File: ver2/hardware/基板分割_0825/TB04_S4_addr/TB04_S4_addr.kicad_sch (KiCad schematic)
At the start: 12 parts, among them J101 USB_C_Receptacle_PowerOnly_6P, SW101 SW_SPDT, U101 74LS157, U102 74HC138

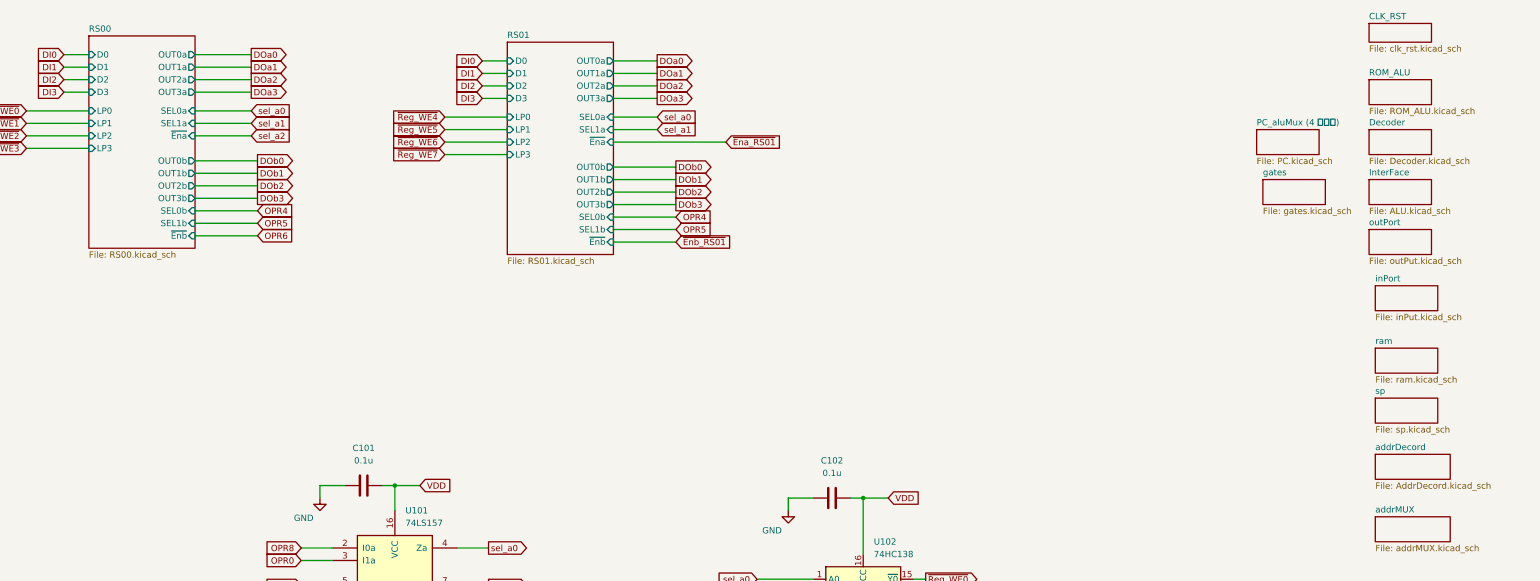
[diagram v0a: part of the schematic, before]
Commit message: ver2: 残り5プロジェクトの不要シートを一括削除
IF表示13/S4 10/S3 11/S1 12/S2 10枚のsheetブロックをS式単位で除去し、
対応する子シート56ファイルを削除。部分削除が要るROM_ALU・PCは残した。
残ったブロックは全てHEADとバイト一致・括弧バランス0を全数確認。

Co-Authored-By: Claude Opus 5 <noreply@anthropic.com>
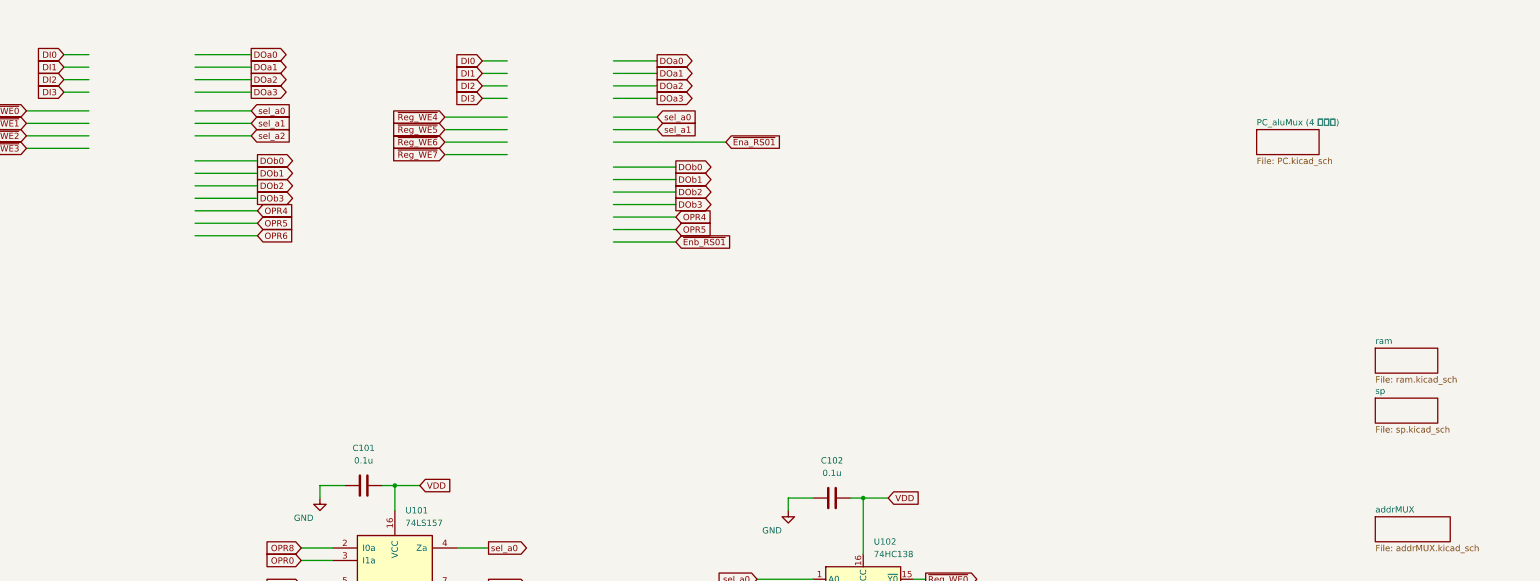
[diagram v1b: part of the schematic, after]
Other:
- removed sheet CLK_RST
- removed sheet Decoder
- removed sheet InterFace
- removed sheet ROM_ALU
- removed sheet RS00
- removed sheet RS01
- removed sheet addrDecord
- removed sheet gates
- removed sheet inPort
- removed sheet outPort

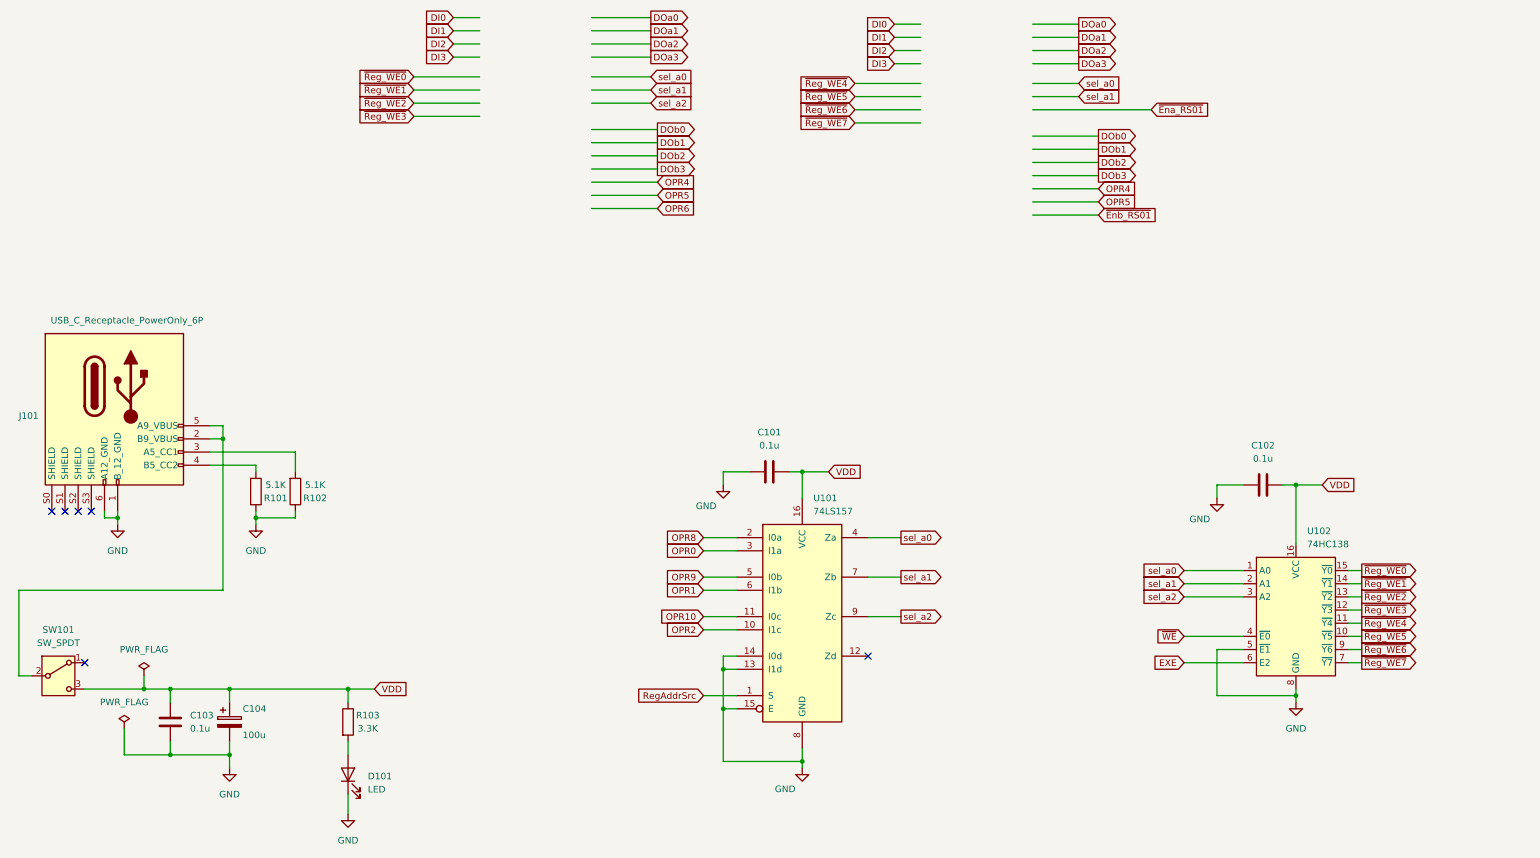
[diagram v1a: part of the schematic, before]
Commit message: ver2: S1-S4のシート内部分削除が完了(署名相違ゼロ)
ROM_ALUをS1(命令ROM側)とS2(ALU ROM・フラグ側)に、PCをS3(ALU入力MUX)と
S4(PC系)に分割。4基板1320ピンをマスターと署名比較して相違0・
ANOMALIES 0。パスコンの員数もIC数と一致(S1 7/S2 17/S3 22/S4 15)。

Co-Authored-By: Claude Opus 5 <noreply@anthropic.com>
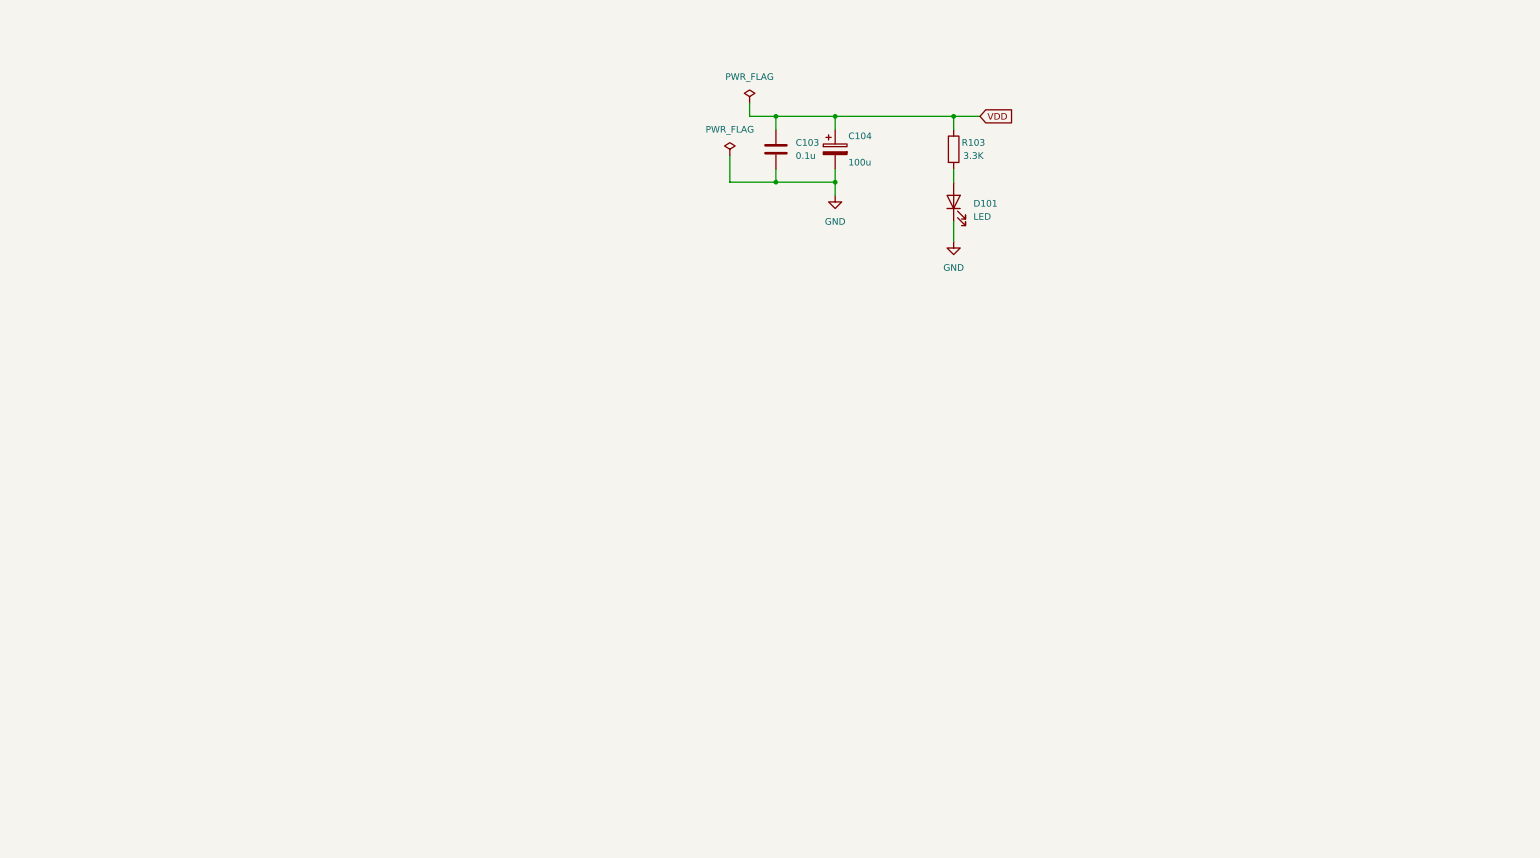
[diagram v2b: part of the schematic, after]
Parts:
- removed C101, C102: 0.1u, Capacitor_THT:C_Disc_D4.3mm_W1.9mm_P5.00mm, symbol Device:C
- removed J101: USB_C_Receptacle_PowerOnly_6P, Library:USB_C_receptacle_onlypower_tanuki, symbol New_Library:USB_C_Receptacle_PowerOnly_6P_tanuki
- removed R101, R102: 5.1K, Resistor_THT:R_Axial_DIN0207_L6.3mm_D2.5mm_P10.16mm_Horizontal, symbol Device:R
- removed SW101: SW_SPDT, Library:sw_slide, symbol Switch:SW_SPDT
- removed U101: 74LS157, symbol 74xx:74LS157
- removed U102: 74HC138, Package_DIP:DIP-16_W7.62mm_Socket, symbol 74xx:74HC138
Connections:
- no-connect marks 6 -> 0
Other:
- moved on the sheet: C103, C104, D101, R103

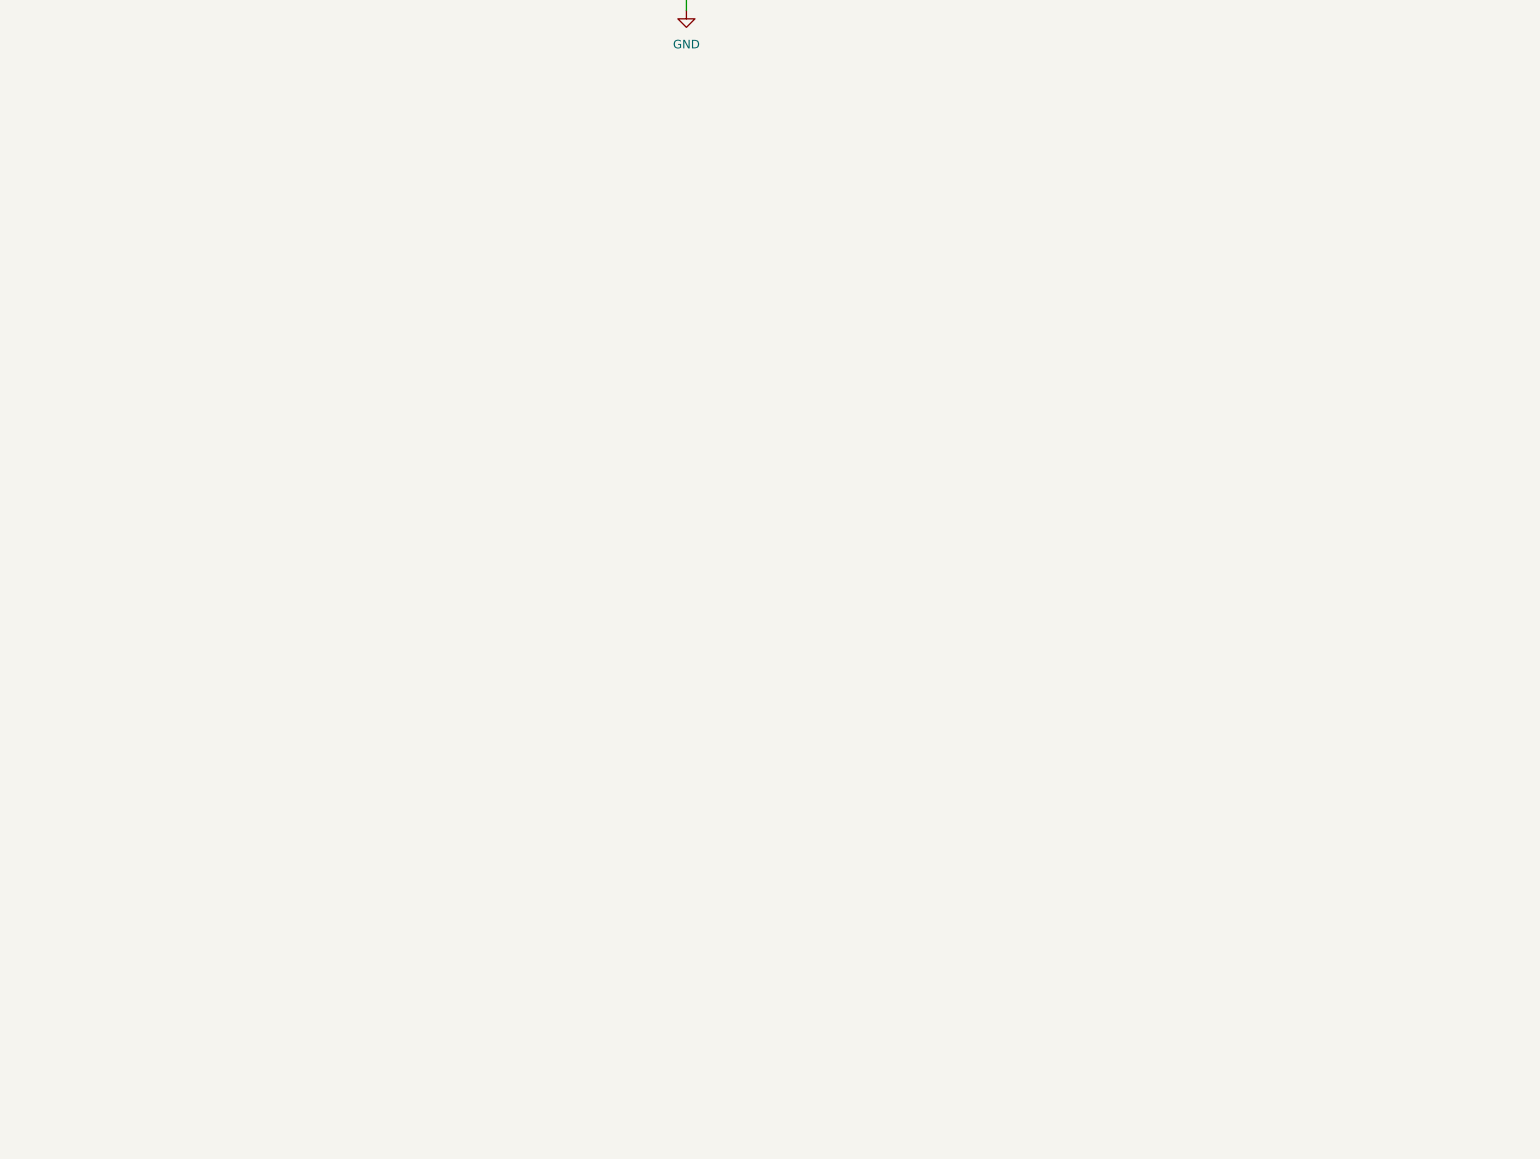
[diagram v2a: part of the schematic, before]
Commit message: ver2: S1-S4にバスヘッダ3本を実装(120ピン全数一致)／S4にIF向け20ピン3個
J101-103は4枚とも確定表と全120ピン一致。J104(IF入力)/J105(IF表示)/
J106(キャリアB)も20ピン全一致。コネクタ以外の署名はマスターと相違0で、
コネクタ追加時のワイヤ吸着なし。PC_Qはバスに載せずJ106のみ。

Co-Authored-By: Claude Opus 5 <noreply@anthropic.com>
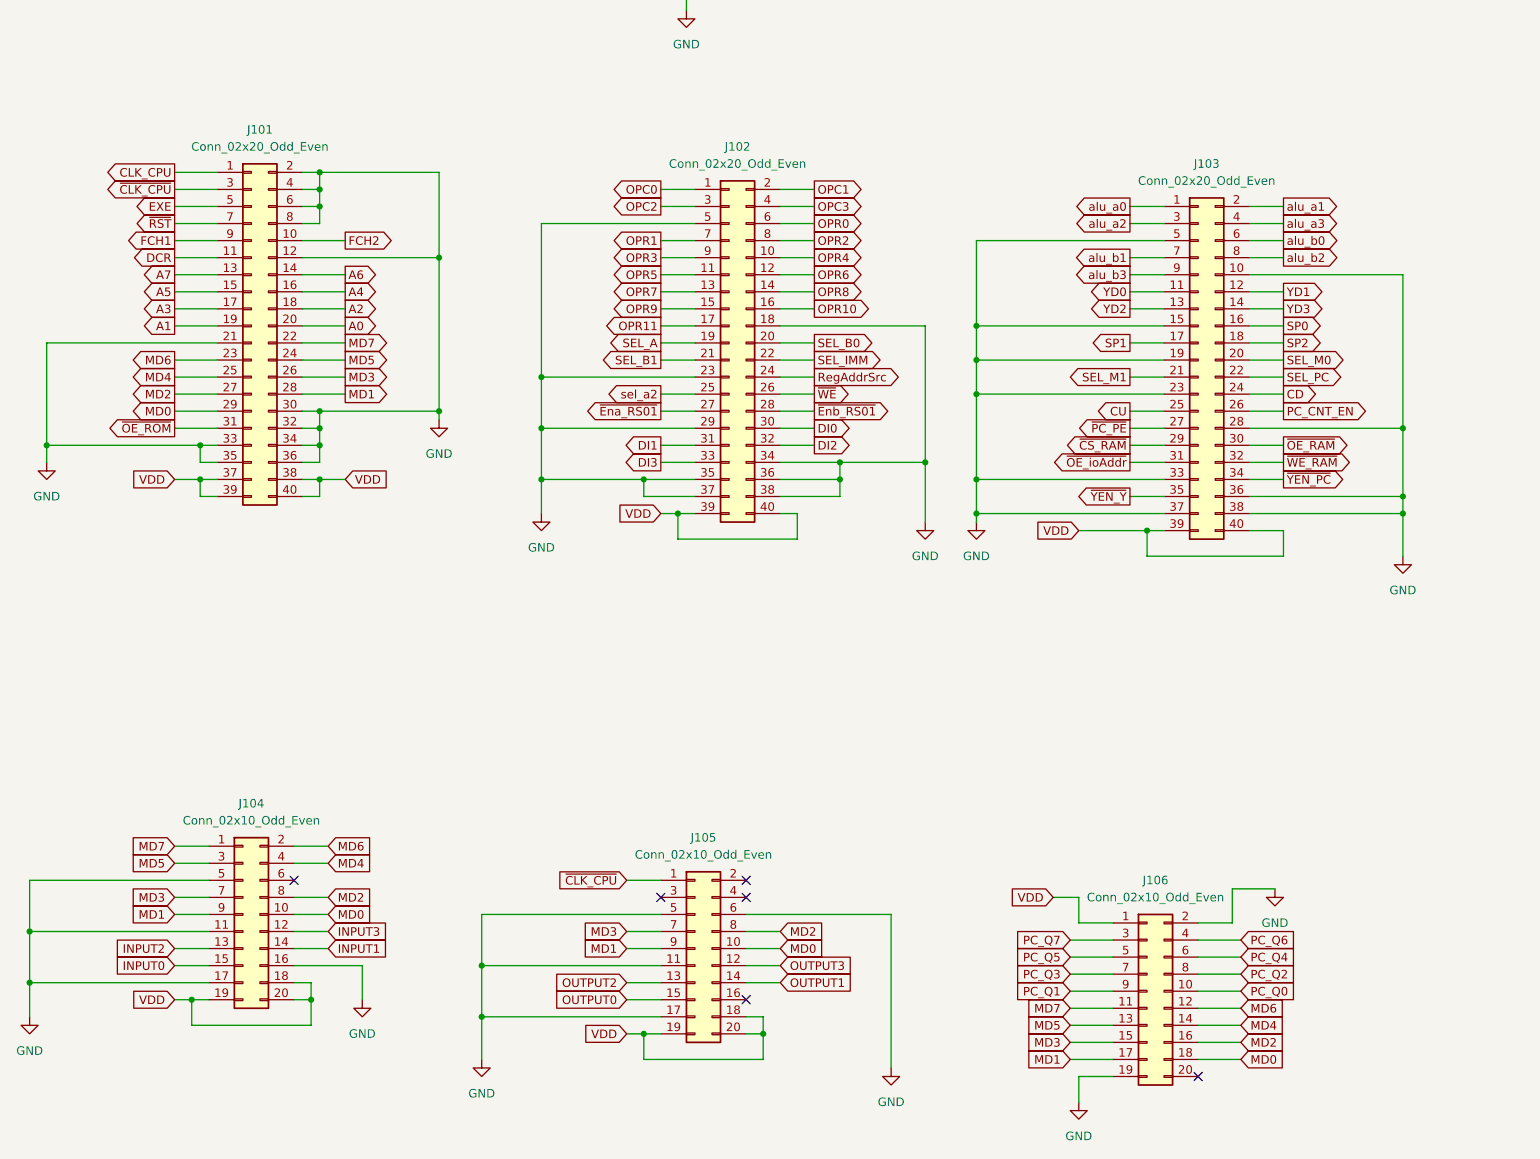
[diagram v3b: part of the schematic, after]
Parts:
- added J101, J102, J103: Conn_02x20_Odd_Even, symbol Connector_Generic:Conn_02x20_Odd_Even
- added J104, J105, J106: Conn_02x10_Odd_Even, symbol Connector_Generic:Conn_02x10_Odd_Even
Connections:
- net GND: now also J101.12 (Pin_12), J101.2 (Pin_2), J101.21 (Pin_21), J101.30 (Pin_30), J101.32 (Pin_32), J101.33 (Pin_33), J101.34 (Pin_34), J101.35 (Pin_35), J101.36 (Pin_36), J101.4 (Pin_4), J101.6 (Pin_6), J101.8 (Pin_8), J102.18 (Pin_18), J102.23 (Pin_23), J102.29 (Pin_29), J102.34 (Pin_34), J102.35 (Pin_35), J102.36 (Pin_36), J102.37 (Pin_37), J102.38 (Pin_38), J102.5 (Pin_5), J103.10 (Pin_10), J103.15 (Pin_15), J103.19 (Pin_19), J103.23 (Pin_23), J103.28 (Pin_28), J103.33 (Pin_33), J103.36 (Pin_36), J103.37 (Pin_37), J103.38 (Pin_38), J103.5 (Pin_5), J104.11 (Pin_11), J104.16 (Pin_16), J104.17 (Pin_17), J104.5 (Pin_5), J105.11 (Pin_11), J105.17 (Pin_17), J105.5 (Pin_5), J105.6 (Pin_6), J106.19 (Pin_19), J106.2 (Pin_2)
- net VDD: now also J101.37 (Pin_37), J101.38 (Pin_38), J101.39 (Pin_39), J101.40 (Pin_40), J102.39 (Pin_39), J102.40 (Pin_40), J103.39 (Pin_39), J103.40 (Pin_40), J104.18 (Pin_18), J104.19 (Pin_19), J104.20 (Pin_20), J105.18 (Pin_18), J105.19 (Pin_19), J105.20 (Pin_20), J106.1 (Pin_1)
- new net A0: J101.20 (Pin_20)
- new net A1: J101.19 (Pin_19)
- new net A2: J101.18 (Pin_18)
- new net A3: J101.17 (Pin_17)
- new net A4: J101.16 (Pin_16)
- new net A5: J101.15 (Pin_15)
- new net A6: J101.14 (Pin_14)
- new net A7: J101.13 (Pin_13)
- new net CD: J103.24 (Pin_24)
- new net CLK_CPU: J101.1 (Pin_1)
- new net CU: J103.25 (Pin_25)
- new net DCR: J101.11 (Pin_11)
- new net DI0: J102.30 (Pin_30)
- new net DI1: J102.31 (Pin_31)
- new net DI2: J102.32 (Pin_32)
- new net DI3: J102.33 (Pin_33)
- new net EXE: J101.5 (Pin_5)
- new net FCH1: J101.9 (Pin_9)
- new net FCH2: J101.10 (Pin_10)
- new net INPUT0: J104.15 (Pin_15)
- new net INPUT1: J104.14 (Pin_14)
- new net INPUT2: J104.13 (Pin_13)
- new net INPUT3: J104.12 (Pin_12)
- new net MD0: J101.29 (Pin_29), J104.10 (Pin_10), J105.10 (Pin_10), J106.18 (Pin_18)
- new net MD1: J101.28 (Pin_28), J104.9 (Pin_9), J105.9 (Pin_9), J106.17 (Pin_17)
- new net MD2: J101.27 (Pin_27), J104.8 (Pin_8), J105.8 (Pin_8), J106.16 (Pin_16)
- new net MD3: J101.26 (Pin_26), J104.7 (Pin_7), J105.7 (Pin_7), J106.15 (Pin_15)
- new net MD4: J101.25 (Pin_25), J104.4 (Pin_4), J106.14 (Pin_14)
- new net MD5: J101.24 (Pin_24), J104.3 (Pin_3), J106.13 (Pin_13)
- new net MD6: J101.23 (Pin_23), J104.2 (Pin_2), J106.12 (Pin_12)
- new net MD7: J101.22 (Pin_22), J104.1 (Pin_1), J106.11 (Pin_11)
- new net OPC0: J102.1 (Pin_1)
- new net OPC1: J102.2 (Pin_2)
- new net OPC2: J102.3 (Pin_3)
- new net OPC3: J102.4 (Pin_4)
- new net OPR0: J102.6 (Pin_6)
- new net OPR1: J102.7 (Pin_7)
- new net OPR10: J102.16 (Pin_16)
- new net OPR11: J102.17 (Pin_17)
- new net OPR2: J102.8 (Pin_8)
- new net OPR3: J102.9 (Pin_9)
- new net OPR4: J102.10 (Pin_10)
- new net OPR5: J102.11 (Pin_11)
- new net OPR6: J102.12 (Pin_12)
- new net OPR7: J102.13 (Pin_13)
- new net OPR8: J102.14 (Pin_14)
- new net OPR9: J102.15 (Pin_15)
- new net OUTPUT0: J105.15 (Pin_15)
- new net OUTPUT1: J105.14 (Pin_14)
- new net OUTPUT2: J105.13 (Pin_13)
- new net OUTPUT3: J105.12 (Pin_12)
- new net PC_CNT_EN: J103.26 (Pin_26)
- new net PC_Q0: J106.10 (Pin_10)
- new net PC_Q1: J106.9 (Pin_9)
- new net PC_Q2: J106.8 (Pin_8)
- new net PC_Q3: J106.7 (Pin_7)
- new net PC_Q4: J106.6 (Pin_6)
- new net PC_Q5: J106.5 (Pin_5)
- new net PC_Q6: J106.4 (Pin_4)
- new net PC_Q7: J106.3 (Pin_3)
- new net RegAddrSrc: J102.24 (Pin_24)
- new net SEL_A: J102.19 (Pin_19)
- new net SEL_B0: J102.20 (Pin_20)
- new net SEL_B1: J102.21 (Pin_21)
- new net SEL_IMM: J102.22 (Pin_22)
- new net SEL_M0: J103.20 (Pin_20)
- new net SEL_M1: J103.21 (Pin_21)
- new net SEL_PC: J103.22 (Pin_22)
- new net SP0: J103.16 (Pin_16)
- new net SP1: J103.17 (Pin_17)
- new net SP2: J103.18 (Pin_18)
- new net YD0: J103.11 (Pin_11)
- new net YD1: J103.12 (Pin_12)
- new net YD2: J103.13 (Pin_13)
- new net YD3: J103.14 (Pin_14)
- new net alu_a0: J103.1 (Pin_1)
- new net alu_a1: J103.2 (Pin_2)
- new net alu_a2: J103.3 (Pin_3)
- new net alu_a3: J103.4 (Pin_4)
- new net alu_b0: J103.6 (Pin_6)
- new net alu_b1: J103.7 (Pin_7)
- new net alu_b2: J103.8 (Pin_8)
- new net alu_b3: J103.9 (Pin_9)
- new net sel_a2: J102.25 (Pin_25)
- new net ~{CLK_CPU}: J101.3 (Pin_3), J105.1 (Pin_1)
- new net ~{CS_RAM}: J103.29 (Pin_29)
- new net ~{Ena_RS01}: J102.27 (Pin_27)
- new net ~{Enb_RS01}: J102.28 (Pin_28)
- new net ~{OE_RAM}: J103.30 (Pin_30)
- new net ~{OE_ROM}: J101.31 (Pin_31)
- new net ~{OE_ioAddr}: J103.31 (Pin_31)
- new net ~{PC_PE}: J103.27 (Pin_27)
- new net ~{RST}: J101.7 (Pin_7)
- new net ~{WE_RAM}: J103.32 (Pin_32)
- new net ~{WE}: J102.26 (Pin_26)
- new net ~{YEN_PC}: J103.34 (Pin_34)
- new net ~{YEN_Y}: J103.35 (Pin_35)
- no-connect marks 0 -> 6
